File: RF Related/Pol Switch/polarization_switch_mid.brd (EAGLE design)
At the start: 88.4 x 54.4 mm, 61 parts, among them IC1 VLPR-24-858-2, IC10 ADP-2-1+_MINICIRCUITS, IC11 ADP-2-1+_MINICIRCUITS, IC12 QCV-151+, IC13 MAX8878EUK28+T, IC14 SN74LVC2G17DBVT, IC15 SN74LVC2G17DBVT, IC2 VLPR-24-858-2, IC3 HSWA2-30DR+, IC4 VLPR-24-858-2, IC5 HSWA2-30DR+, IC6 HSWA2-30DR+, IC7 HSWA2-30DR+, IC8 PHA-13LN+, IC9 PHA-13LN+, J1 M20-9730645, J2 171856-0002, X3 SMA-142-0701-801/806, X4 SMA-142-0701-801/806, X5 SMA-142-0701-801/806

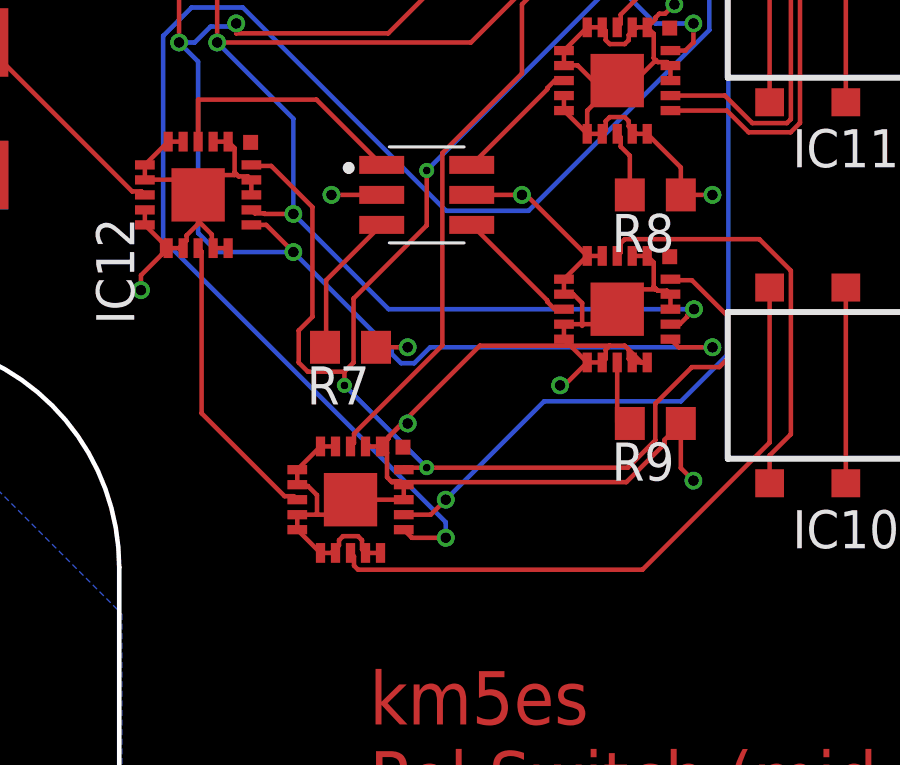
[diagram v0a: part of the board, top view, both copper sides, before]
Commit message: redoing the routing again for pol switch. making backup now.
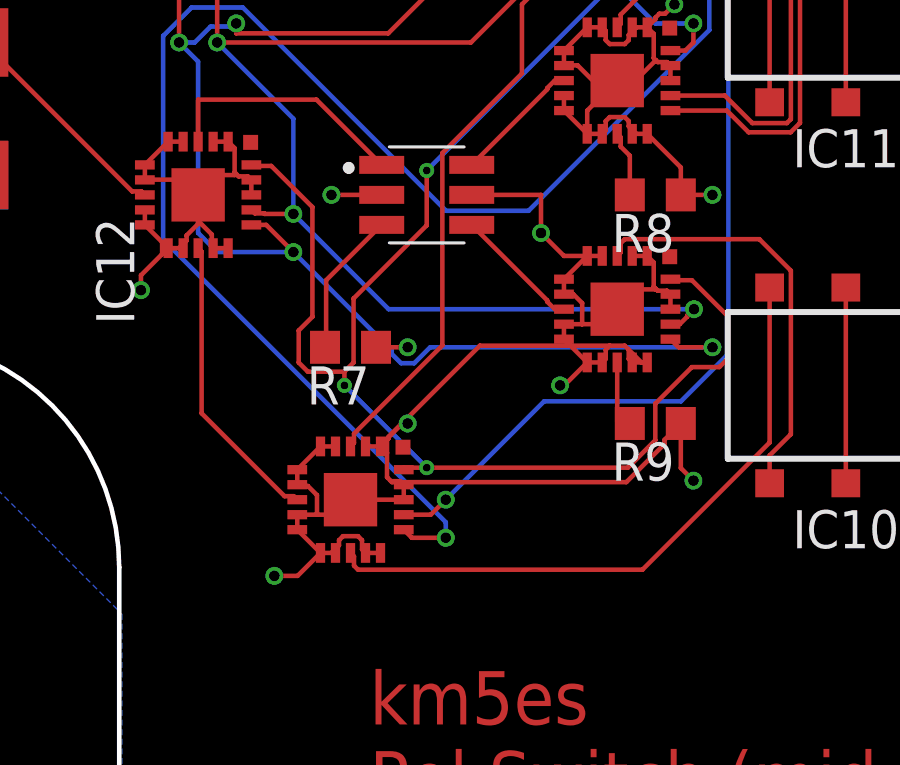
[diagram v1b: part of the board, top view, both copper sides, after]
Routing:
- net GND: track 190.2 -> 192.4 mm, vias 54 -> 55
- net N$19: track 2.80 -> 2.21 mm
